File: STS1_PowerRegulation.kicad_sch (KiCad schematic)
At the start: 28 parts, among them U24 MCP1725-3302E_MC, U3 MCP1725-3302E_MC

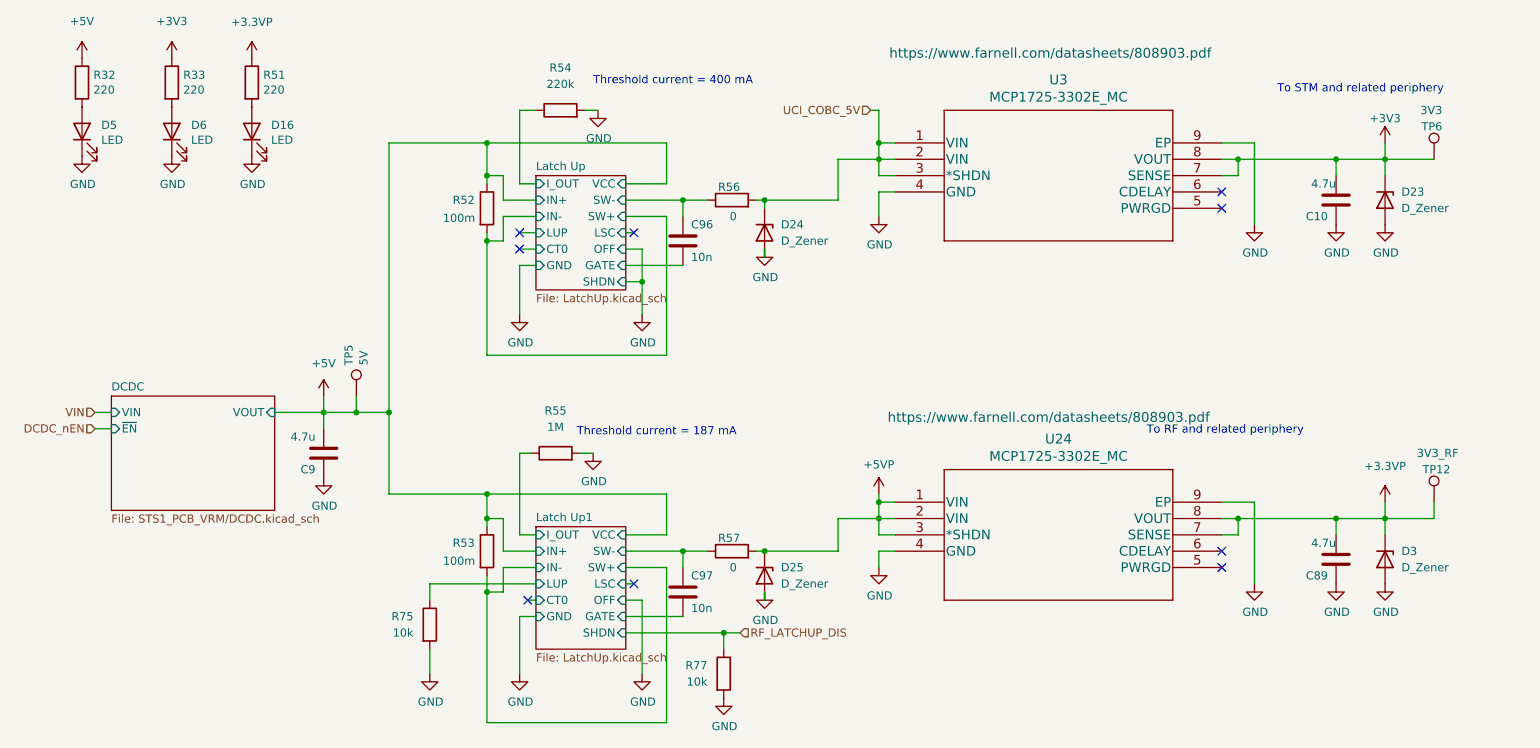
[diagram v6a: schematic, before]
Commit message: Add a couple of Zener diodes to protect inputs of MOSFETs
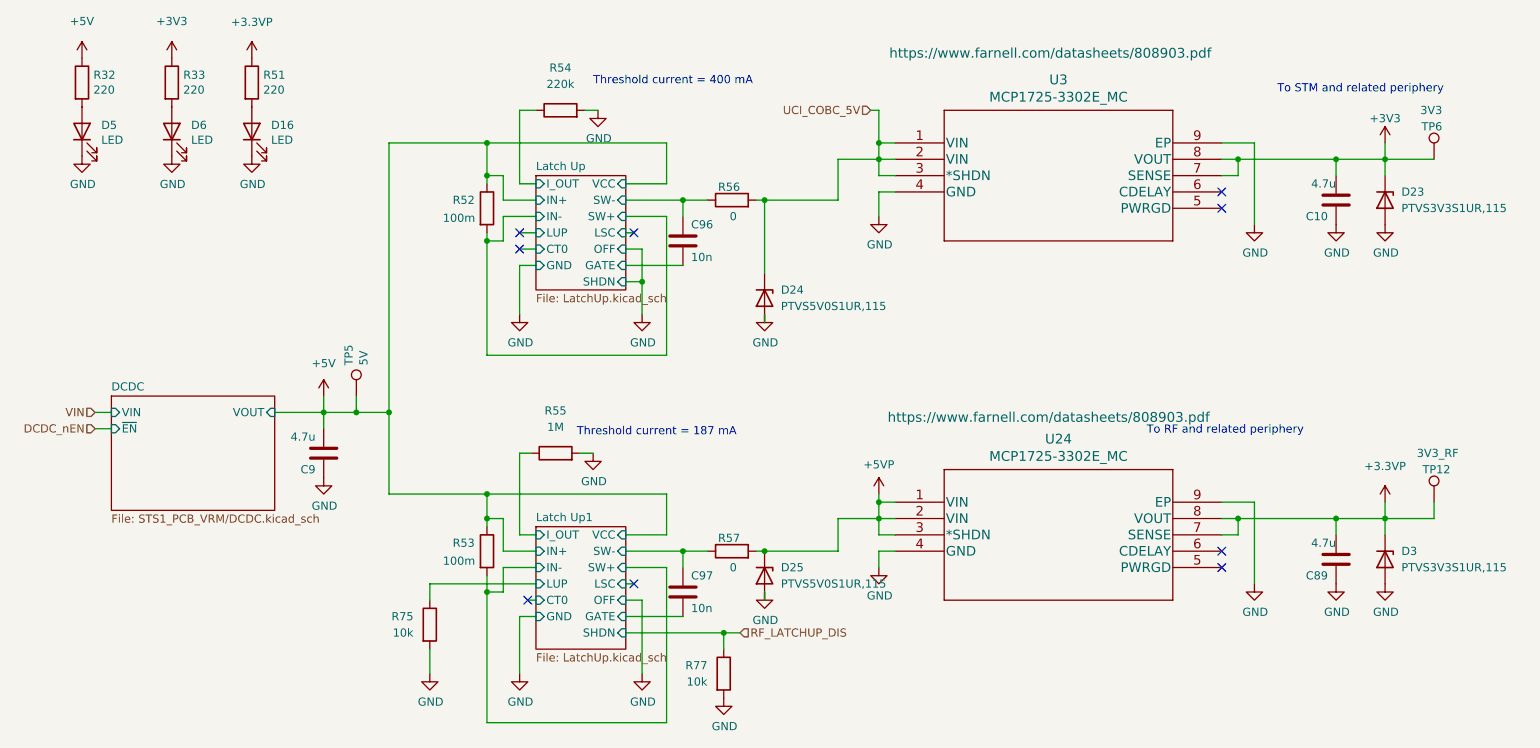
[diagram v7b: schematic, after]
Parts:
- D23, D3: value D_Zener -> PTVS3V3S1UR,115
- D24, D25: value D_Zener -> PTVS5V0S1UR,115
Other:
- moved on the sheet: D24
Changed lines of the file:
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@@
     (stroke (width 0) (type default) (color 0 0 0 0))
   )
-  (wire (pts (xy 138.43 48.26) (xy 138.43 46.99))
+  (wire (pts (xy 138.43 58.42) (xy 138.43 46.99))
     (stroke (width 0) (type default) (color 0 0 0 0))
   )
@@
     (stroke (width 0) (type default) (color 0 0 0 0))
   )
-  (wire (pts (xy 138.43 55.88) (xy 138.43 54.61))
+  (wire (pts (xy 138.43 66.04) (xy 138.43 64.77))
     (stroke (width 0) (type default) (color 0 0 0 0))
   )
@@
       (effects (font (size 1.27 1.27)) (justify left))
     )
-    (property "Value" "D_Zener" (id 1) (at 237.49 104.1399 90)
+    (property "Value" "PTVS3V3S1UR,115" (id 1) (at 237.49 104.1399 90)
       (effects (font (size 1.27 1.27)) (justify left))
     )
@@
     (pin "1")
   )
-  (symbol (lib_id "power:GND") (at 138.43 54.61 0) (unit 1)
-    (in_bom yes) (on_board yes)
-    (property "Reference" "#PWR0161" (id 0) (at 138.43 60.96 0)
-      (effects (font (size 1.27 1.27)) hide)
-    )
-    (property "Value" "GND" (id 1) (at 138.557 59.0042 0))
-    (property "Footprint" "" (id 2) (at 138.43 54.61 0)
-      (effects (font (size 1.27 1.27)) hide)
-    )
-    (property "Datasheet" "" (id 3) (at 138.43 54.61 0)
+  (symbol (lib_id "power:GND") (at 138.43 64.77 0) (unit 1)
+    (in_bom yes) (on_board yes)
+    (property "Reference" "#PWR0161" (id 0) (at 138.43 71.12 0)
+      (effects (font (size 1.27 1.27)) hide)
+    )
+    (property "Value" "GND" (id 1) (at 138.557 69.1642 0))
+    (property "Footprint" "" (id 2) (at 138.43 64.77 0)
+      (effects (font (size 1.27 1.27)) hide)
+    )
+    (property "Datasheet" "" (id 3) (at 138.43 64.77 0)
       (effects (font (size 1.27 1.27)) hide)
     )
@@
       (effects (font (size 1.27 1.27)) (justify left))
     )
-    (property "Value" "D_Zener" (id 1) (at 237.49 48.2599 90)
+    (property "Value" "PTVS3V3S1UR,115" (id 1) (at 237.49 48.2599 90)
       (effects (font (size 1.27 1.27)) (justify left))
     )
@@
     (pin "2")
   )
-  (symbol (lib_id "Device:D_Zener") (at 138.43 52.07 270) (unit 1)
+  (symbol (lib_id "Device:D_Zener") (at 138.43 62.23 270) (unit 1)
     (in_bom yes) (on_board yes) (fields_autoplaced)
-    (property "Reference" "D24" (id 0) (at 140.97 50.7999 90)
-      (effects (font (size 1.27 1.27)) (justify left))
-    )
-    (property "Value" "D_Zener" (id 1) (at 140.97 53.3399 90)
-      (effects (font (size 1.27 1.27)) (justify left))
-    )
-    (property "Footprint" "Diode_SMD:D_SOD-123" (id 2) (at 138.43 52.07 0)
-      (effects (font (size 1.27 1.27)) hide)
-    )
-    (property "Datasheet" "~" (id 3) (at 138.43 52.07 0)
-      (effects (font (size 1.27 1.27)) hide)
-    )
-    (property "JLCPCB Part #" "C478011" (id 4) (at 138.43 52.07 0)
-      (effects (font (size 1.27 1.27)) hide)
-    )
-    (property "Manufacturer_Part_Number" "PTVS5V0S1UR,115 " (id 5) (at 138.43 52.07 0)
+    (property "Reference" "D24" (id 0) (at 140.97 60.9599 90)
+      (effects (font (size 1.27 1.27)) (justify left))
+    )
+    (property "Value" "PTVS5V0S1UR,115 " (id 1) (at 140.97 63.4999 90)
+      (effects (font (size 1.27 1.27)) (justify left))
+    )
+    (property "Footprint" "Diode_SMD:D_SOD-123" (id 2) (at 138.43 62.23 0)
+      (effects (font (size 1.27 1.27)) hide)
+    )
+    (property "Datasheet" "~" (id 3) (at 138.43 62.23 0)
+      (effects (font (size 1.27 1.27)) hide)
+    )
+    (property "JLCPCB Part #" "C478011" (id 4) (at 138.43 62.23 0)
+      (effects (font (size 1.27 1.27)) hide)
+    )
+    (property "Manufacturer_Part_Number" "PTVS5V0S1UR,115 " (id 5) (at 138.43 62.23 0)
       (effects (font (size 1.27 1.27)) hide)
     )
@@
       (effects (font (size 1.27 1.27)) (justify left))
     )
-    (property "Value" "D_Zener" (id 1) (at 140.97 106.6799 90)
-      (effects (font (size 1.27 1.27)) (justify left))
+    (property "Value" "PTVS5V0S1UR,115" (id 1) (at 140.97 106.6799 90)
+      (effects (font (size 0 0)) (justify left))
     )
     (property "Footprint" "Diode_SMD:D_SOD-123" (id 2) (at 138.43 105.41 0)

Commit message: Update the manufacturer part number for some of components to be compatible with avaiable parts in the JLC parts database
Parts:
- C10, C89, C9: JLCPCB Part # C5969198 -> C338087; Manufacturer_Part_Number CL10A475KP8NNWC -> CGA3E1X5R0J475KT0Y0E
- C96, C97: JLCPCB Part # C307477 -> C2180616; Manufacturer_Part_Number CL10B103KB8NFNC -> C0603C103M5RACAUTO
- D16, D5, D6: JLCPCB Part # (none) -> C165984; Manufacturer_Part_Number 598-8160-107F -> BL-HGE35A-AV-TRB
- U24: Manufacturer_Part_Number MCP1725-3302E/MC -> MCP1725-3302E/MC
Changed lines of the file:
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@@
       (effects (font (size 1.27 1.27)) hide)
     )
-    (property "JLCPCB Part #" "C5969198" (id 4) (at 69.85 86.36 0)
-      (effects (font (size 1.27 1.27)) hide)
-    )
-    (property "Manufacturer_Part_Number" "CL10A475KP8NNWC " (id 5) (at 69.85 86.36 0)
+    (property "JLCPCB Part #" "C338087" (id 4) (at 69.85 86.36 0)
+      (effects (font (size 1.27 1.27)) hide)
+    )
+    (property "Manufacturer_Part_Number" "CGA3E1X5R0J475KT0Y0E" (id 5) (at 69.85 86.36 0)
       (effects (font (size 1.27 1.27)) hide)
     )
@@
       (effects (font (size 1.27 1.27)) hide)
     )
-    (property "JLCPCB Part #" "C5969198" (id 4) (at 227.33 46.99 0)
-      (effects (font (size 1.27 1.27)) hide)
-    )
-    (property "Manufacturer_Part_Number" "CL10A475KP8NNWC " (id 5) (at 227.33 46.99 0)
+    (property "JLCPCB Part #" "C338087" (id 4) (at 227.33 46.99 0)
+      (effects (font (size 1.27 1.27)) hide)
+    )
+    (property "Manufacturer_Part_Number" "CGA3E1X5R0J475KT0Y0E" (id 5) (at 227.33 46.99 0)
       (effects (font (size 1.27 1.27)) hide)
     )
@@
       (effects (font (size 1.27 1.27)) hide)
     )
-    (property "Manufacturer_Part_Number" "598-8160-107F " (id 4) (at 58.674 36.322 90)
-      (effects (font (size 1.27 1.27)) hide)
-    )
-    (property "JLCPCB Part #" "" (id 5) (at 58.674 36.322 90)
+    (property "Manufacturer_Part_Number" "BL-HGE35A-AV-TRB" (id 4) (at 58.674 36.322 90)
+      (effects (font (size 1.27 1.27)) hide)
+    )
+    (property "JLCPCB Part #" "C165984" (id 5) (at 58.674 36.322 90)
       (effects (font (size 1.27 1.27)) hide)
     )
@@
       (effects (font (size 1.27 1.27)) hide)
     )
-    (property "JLCPCB Part #" "C5969198" (id 4) (at 227.33 102.87 0)
-      (effects (font (size 1.27 1.27)) hide)
-    )
-    (property "Manufacturer_Part_Number" "CL10A475KP8NNWC " (id 5) (at 227.33 102.87 0)
+    (property "JLCPCB Part #" "C338087" (id 4) (at 227.33 102.87 0)
+      (effects (font (size 1.27 1.27)) hide)
+    )
+    (property "Manufacturer_Part_Number" "CGA3E1X5R0J475KT0Y0E" (id 5) (at 227.33 102.87 0)
       (effects (font (size 1.27 1.27)) hide)
     )
@@
       (effects (font (size 1.27 1.27)) hide)
     )
-    (property "Manufacturer_Part_Number" "598-8160-107F " (id 4) (at 32.258 36.322 90)
-      (effects (font (size 1.27 1.27)) hide)
-    )
-    (property "JLCPCB Part #" "" (id 5) (at 32.258 36.322 90)
+    (property "Manufacturer_Part_Number" "BL-HGE35A-AV-TRB" (id 4) (at 32.258 36.322 90)
+      (effects (font (size 1.27 1.27)) hide)
+    )
+    (property "JLCPCB Part #" "C165984" (id 5) (at 32.258 36.322 90)
       (effects (font (size 1.27 1.27)) hide)
     )
@@
       (effects (font (size 1.524 1.524)))
     )
-    (property "Manufacturer_Part_Number" "MCP1725-3302E/MC" (id 4) (at 158.75 93.98 0)
+    (property "Manufacturer_Part_Number" "MCP1725-3302E/MC " (id 4) (at 158.75 93.98 0)
       (effects (font (size 1.27 1.27)) hide)
     )
@@
       (effects (font (size 1.27 1.27)) hide)
     )
-    (property "Manufacturer_Part_Number" "598-8160-107F " (id 4) (at 46.228 36.322 90)
-      (effects (font (size 1.27 1.27)) hide)
-    )
-    (property "JLCPCB Part #" "" (id 5) (at 46.228 36.322 90)
+    (property "Manufacturer_Part_Number" "BL-HGE35A-AV-TRB" (id 4) (at 46.228 36.322 90)
+      (effects (font (size 1.27 1.27)) hide)
+    )
+    (property "JLCPCB Part #" "C165984" (id 5) (at 46.228 36.322 90)
       (effects (font (size 1.27 1.27)) hide)
     )
@@
       (effects (font (size 1.27 1.27)) hide)
     )
-    (property "JLCPCB Part #" "C307477" (id 4) (at 125.73 53.34 0)
-      (effects (font (size 1.27 1.27)) hide)
-    )
-    (property "Manufacturer_Part_Number" "CL10B103KB8NFNC " (id 5) (at 125.73 53.34 0)
+    (property "JLCPCB Part #" "C2180616" (id 4) (at 125.73 53.34 0)
+      (effects (font (size 1.27 1.27)) hide)
+    )
+    (property "Manufacturer_Part_Number" "C0603C103M5RACAUTO" (id 5) (at 125.73 53.34 0)
       (effects (font (size 1.27 1.27)) hide)
     )
@@
       (effects (font (size 1.27 1.27)) hide)
     )
-    (property "JLCPCB Part #" "C307477" (id 4) (at 125.73 107.95 0)
-      (effects (font (size 1.27 1.27)) hide)
-    )
-    (property "Manufacturer_Part_Number" "CL10B103KB8NFNC " (id 5) (at 125.73 107.95 0)
-      (effects (font (size 1.27 1.27)) hide)
-    )
+    (property "JLCPCB Part #" "C2180616" (id 4) (at 125.73 107.95 0)
+      (effects (font (size 1.27 1.27)) hide)
+    )
+    (property "Manufacturer_Part_Number" "C0603C103M5RACAUTO" (id 5) (at 125.73 107.95 0)
+      (effects (font (size 1.27 1.27)) hide)
+    )
